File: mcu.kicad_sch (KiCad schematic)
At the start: 24 parts, among them J1 Bus_M.2_Socket_E, J2 Conn_01x04_Socket, U1 STM8S003F3P, U5 ISO7741N1-Y, U6 CS817X20LS, U7 AMS1117-3.3

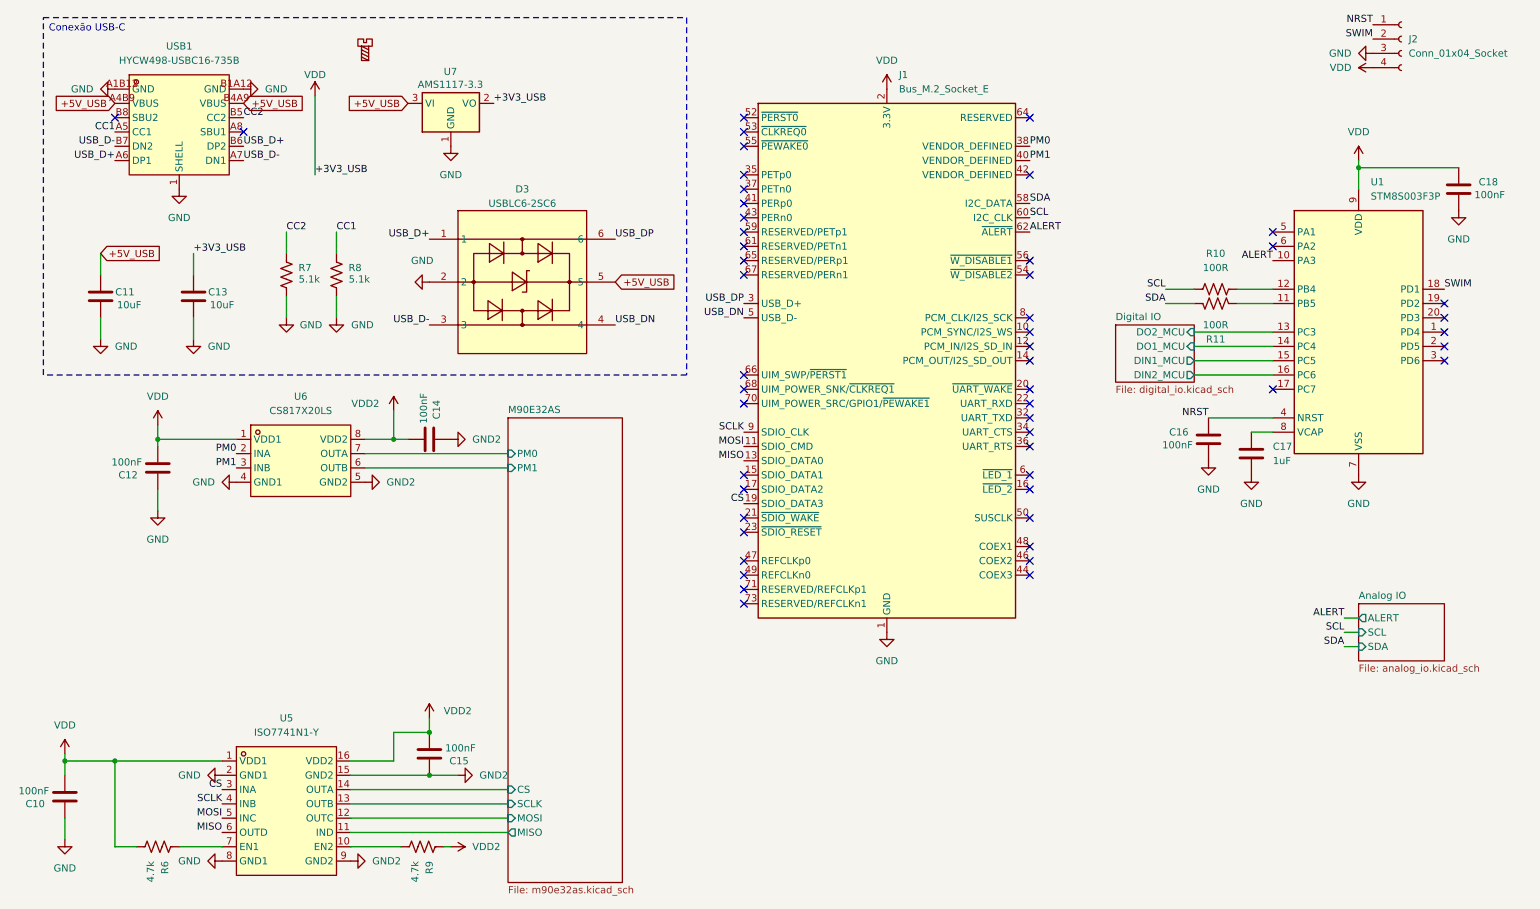
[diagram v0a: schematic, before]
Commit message: Migra componentes das bibliotecas LCSC locais para pecas JLCPCB
Troca os part numbers para casar com o estoque da JLCPCB e com o
catalogo PCBA Basic, eliminando a biblioteca local que era importada
via easyeda2kicad.

- Remove libraries/ (simbolos, footprints e modelos 3D importados) e o
  script import_lcsc_component.sh
- Adiciona o plugin JLCPCB (jlcpcb/project.db) e os scripts auxiliares
  fix_jlcpcb_tools_deps.sh e generate_ibom.sh
- Atualiza as cinco folhas do esquematico, o PCB e as regras de projeto

O PCB fica em estado intermediario: os componentes novos ainda precisam
ser reposicionados e as trilhas refeitas.

Co-Authored-By: Claude Opus 5 (1M context) <noreply@anthropic.com>
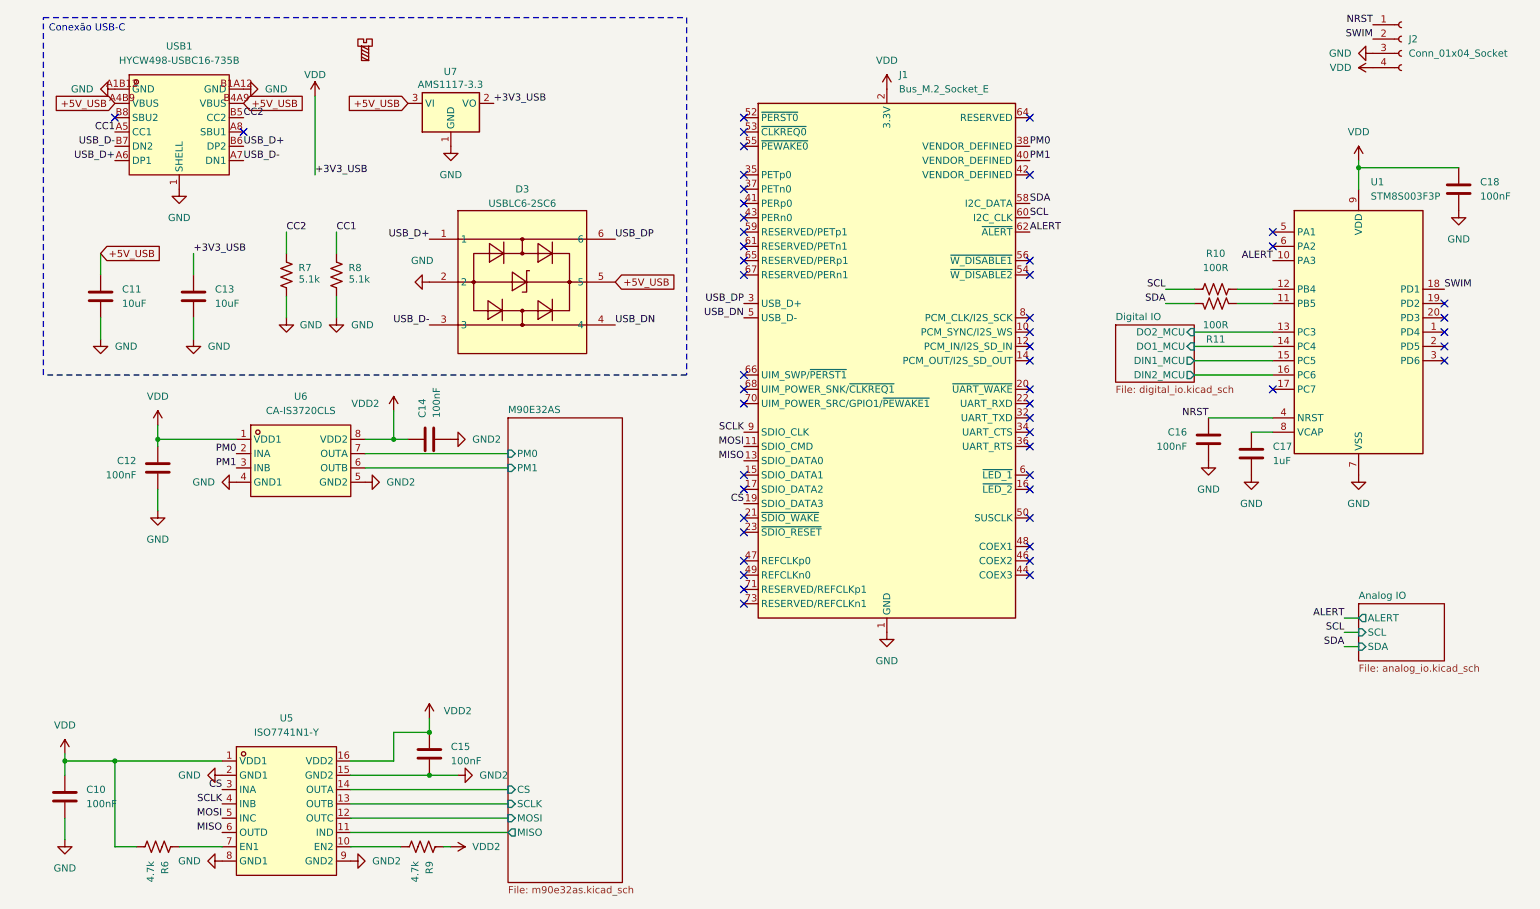
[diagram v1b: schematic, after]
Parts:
- C10, C12, C14, C15, C16, C18: footprint Capacitor_SMD:C_0201_0603Metric -> Capacitor_SMD:C_0402_1005Metric; JLCPCB Part # (none) -> C1525; LCSC Part # C7393837 -> (none); MPN TCC0201X7R104K100ZT -> CL05B104KO5NNNC
- C11, C13: footprint Capacitor_SMD:C_0603_1608Metric -> Capacitor_SMD:C_0402_1005Metric; JLCPCB Part # (none) -> C15525; LCSC Part # C6119842 -> (none); MPN CGA0603X5R106K100JT -> CL05A106MQ5NUNC
- C17: JLCPCB Part # (none) -> C52923; LCSC Part # C301999 -> (none); MPN 0402X105M6R3NT -> CL05A105KA5NQNC
- D3: JLCPCB Part # (none) -> C7519; LCSC Part # C7519 -> (none)
- J1: JLCPCB Part # (none) -> C410527; LCSC Part # C410527 -> (none)
- R10, R11: JLCPCB Part # (none) -> C25076; LCSC Part # C54920613 -> (none); MPN HRC0402F1000DNTO -> 0402WGF1000TCE
- R6, R9: JLCPCB Part # (none) -> C25900; LCSC Part # C3017492 -> (none); MPN SCR0402J4K7 -> 0402WGF4701TCE
- R7, R8: JLCPCB Part # (none) -> C384321; LCSC Part # C384321 -> (none)
- U1: JLCPCB Part # (none) -> C52717; LCSC Part # C52717 -> (none)
- U5: JLCPCB Part # (none) -> C53446593; LCSC Part # C53446593 -> (none); Manufacturer YLPTEC(易川) -> (none)
- U6: value CS817X20LS -> CA-IS3720CLS; JLCPCB Part # (none) -> C41784134; LCSC Part # C5561839 -> (none); MPN CS817x20LS -> CA-IS3720CLS; Manufacturer Chipanalog(川土微) -> (none)
- U7: JLCPCB Part # (none) -> C50313802; LCSC Part # C50313802 -> (none)
- USB1: JLCPCB Part # (none) -> C42400252; LCSC Part # C42400252 -> (none)
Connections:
- net +5V_USB: now also C11.1; no longer C11.2
- net GND: now also C10.2, C11.2, C12.2, C13.2; no longer C10.1, C11.1, C12.1, C13.1
- net GND2: now also C14.2, C15.2; no longer C14.1, C15.1
- net VDD: now also C10.1, C12.1, C13.1; no longer C10.2, C12.2, C13.2
- net VDD2: now also C14.1, C15.1; no longer C14.2, C15.2

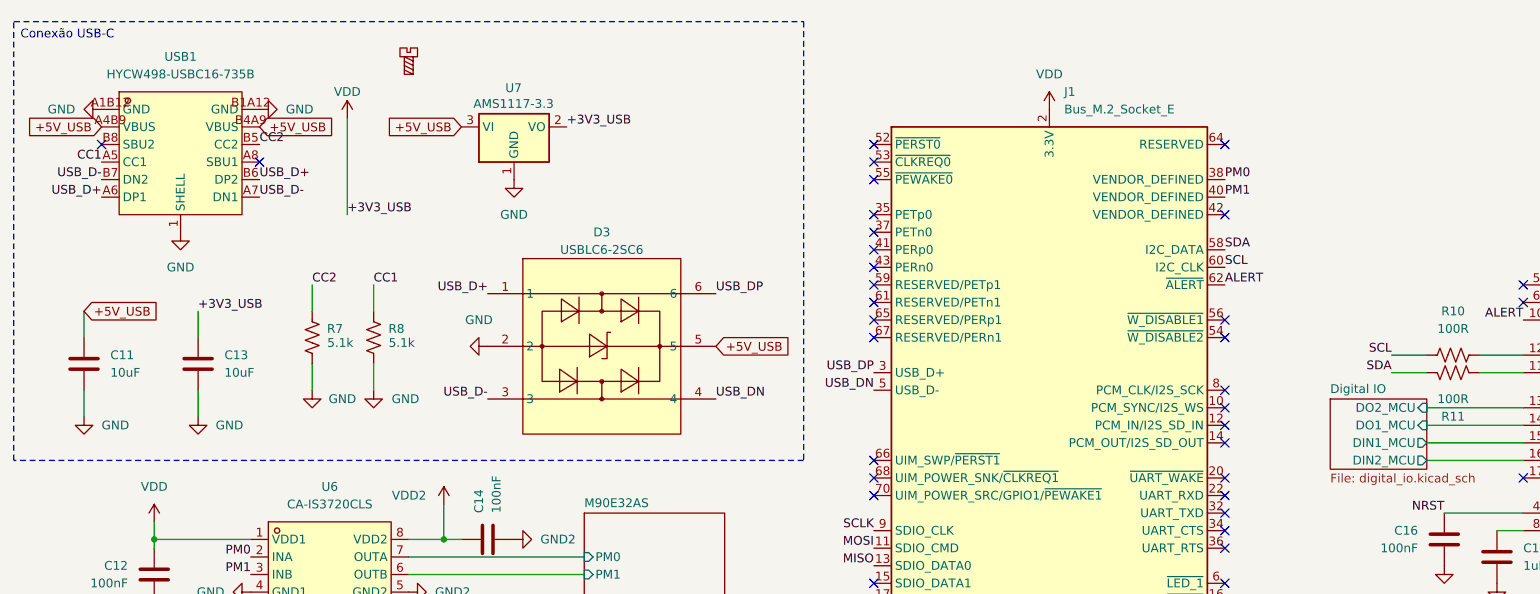
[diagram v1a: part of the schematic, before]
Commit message: Reintroduz biblioteca local ra5_2022 e atualiza layout/esquematicos
Volta a usar simbolos, footprints e modelos 3D importados via
easyeda2kicad (libraries/) em vez das pecas basicas JLCPCB adotadas no
commit anterior, alem de atualizar o roteamento/posicionamento no PCB
e as cinco folhas do esquematico.

Co-Authored-By: Claude Sonnet 5 <noreply@anthropic.com>
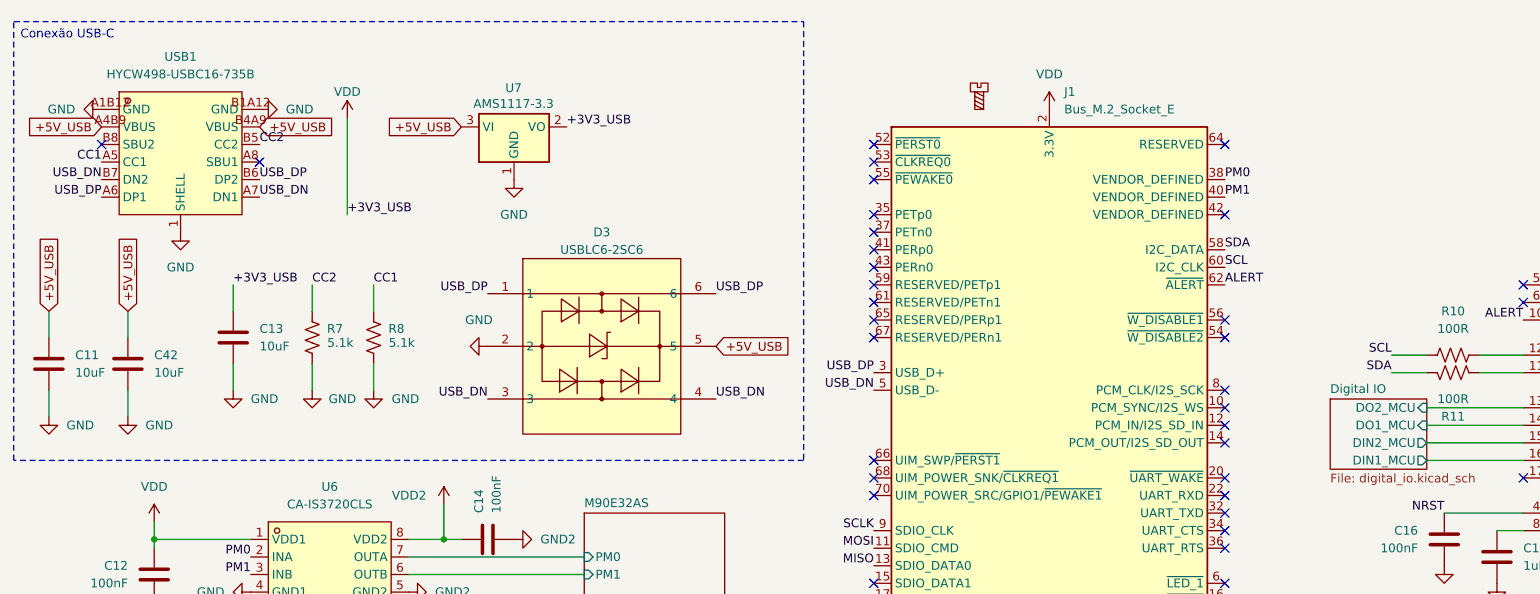
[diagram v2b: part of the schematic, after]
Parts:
- added C42: 10uF, Capacitor_SMD:C_0402_1005Metric, symbol Device:C
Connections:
- net USB_D+ is gone; now on net USB_DP: D3.1, USB1.A6 (DP1), USB1.B6 (DP2)
- net USB_D- is gone; now on net USB_DN: D3.3, USB1.A7 (DN1), USB1.B7 (DN2)
- net +5V_USB: now also C42.1
- net Digital IO/DIN1_MCU: now also U1.16 (PC6); no longer U1.15 (PC5)
- net Digital IO/DIN2_MCU: now also U1.15 (PC5); no longer U1.16 (PC6)
- net GND: now also C42.2
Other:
- moved on the sheet: C11, C13
